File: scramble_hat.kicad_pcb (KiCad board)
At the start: 4 copper layers, 51.4 x 21.1 mm, 57 parts, among them J1 NCJ6FA-H, J2 TRRS PJ-3X4S (CTIA, bottom-si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, J3 Carrier LEFT 1-7, J4 Carrier RIGHT 1-7, J5 VDD_PoE / PGND, J6 I2C 3V3/AGND/SDA/SCL, K1 KAQY214S, K2 KAQY214S, Q1 DMP3098 (P-FET 60V), SW1 SS-12D00-G3, U1 ES8389, U2 TPS7A2033

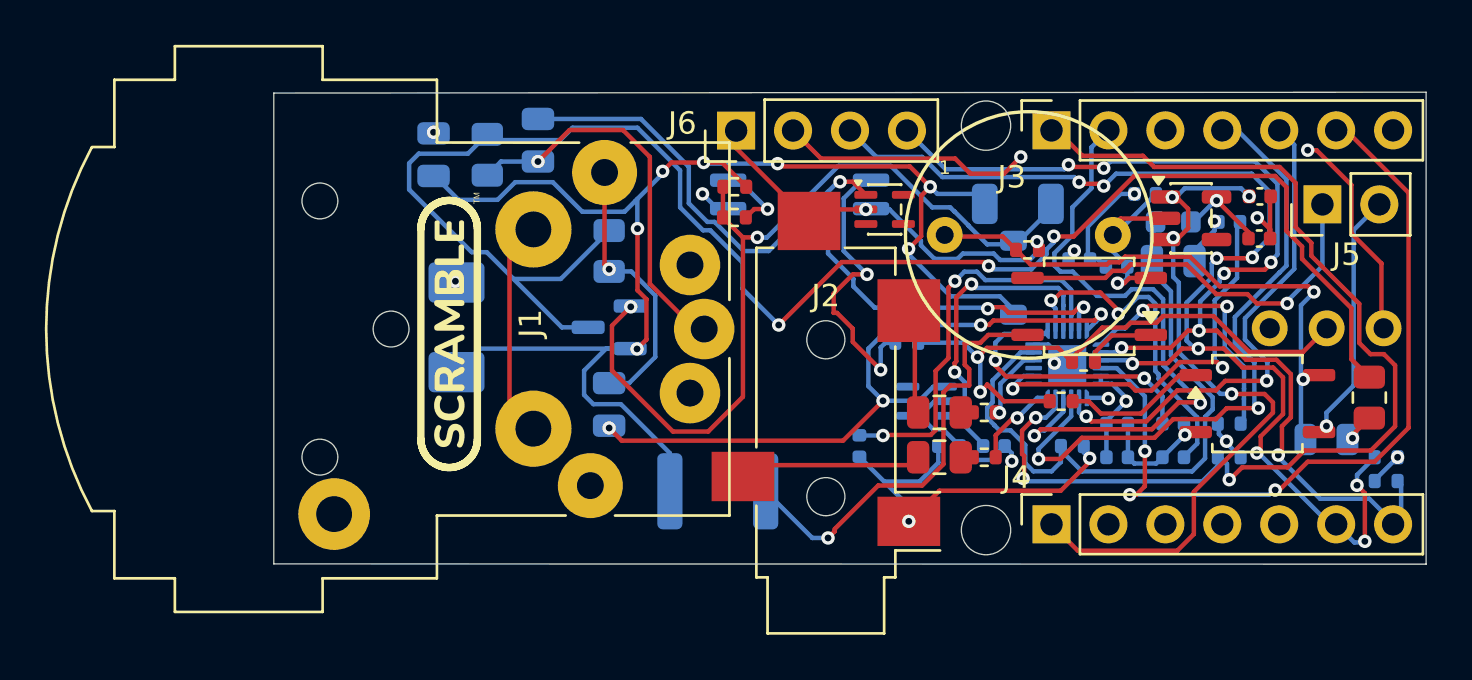
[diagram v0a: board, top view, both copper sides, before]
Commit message: pcb: place + route guitar input; regen fab
Layout for the guitar-input rev (U3 buffer, U4 mux, D9 tip ESD,
R19-R26/C23-C29, D1/D2 now SOD-323). Verified: DRC 0 errors /
0 unconnected, schematic sync clean (75 comps / 61 nets both sides).

Post-layout fixes:
- restore exclude_from_pos_files on C19/J1/J2/J5 (wiped again by
  re-layout; CPL correctly excludes C19,J1,J2,J5,R14)
- point D9 at the project-local 3D model (stock lib ships none)
- remove stale OK1_LED_A routing left from the mis-wired-label detour
  (1 via + 10 segments, all dangling; net verified intact throughout)

fab/ regenerated: gerbers/drills/zip, BOM 34 assembled, CPL 70 placed.
Order-time checks in the JLCPCB preview: U1 QFN (+270) first, then U4
TSSOP-16 (no rotation pattern) and K1/K2 SOP-4 (-90). D1/D2/D9 are
bidirectional two-terminal parts - rotation is not a concern.
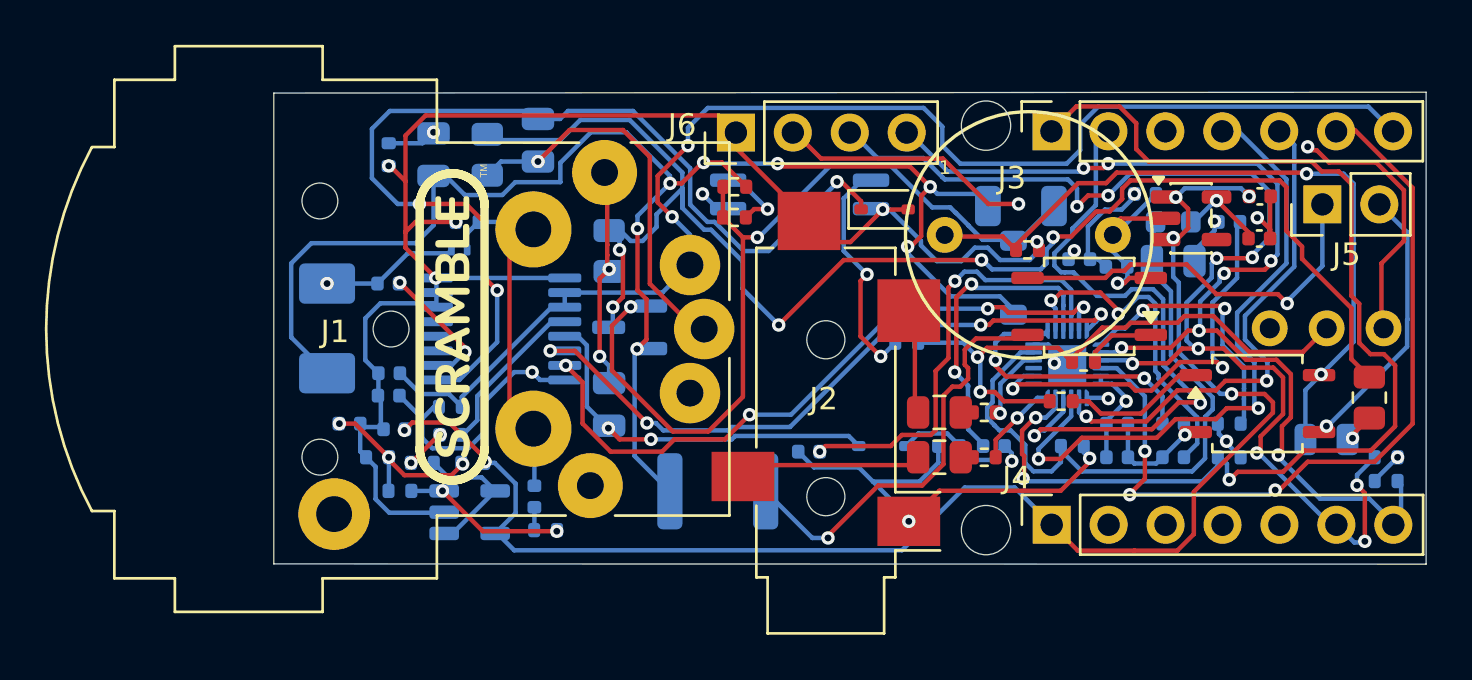
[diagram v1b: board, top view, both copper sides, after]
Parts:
- added C23: 1uF, Capacitor_SMD:C_0402_1005Metric, B.Cu at (92.5, 98.2)
- added C24: 1uF, Capacitor_SMD:C_0402_1005Metric, B.Cu at (84.2, 95.0)
- added C25: 1uF, Capacitor_SMD:C_0402_1005Metric, B.Cu at (88.8, 95.5)
- added C26: 1uF, Capacitor_SMD:C_0402_1005Metric, B.Cu at (86.0, 88.8)
- added C27: 100nF, Capacitor_SMD:C_0402_1005Metric, B.Cu at (86.0, 92.8)
- added C28: 100nF, Capacitor_SMD:C_0402_1005Metric, B.Cu at (86.2, 95.2)
- added C29: 100nF, Capacitor_SMD:C_0402_1005Metric, B.Cu at (86.0, 93.8)
- added D9: TPD1E10B06 (ESD), Package_SON:Texas_DPY0002A_0.6x1mm_P0.65mm, B.Cu at (89.2, 87.2)
- added R19: 100k, Resistor_SMD:R_0402_1005Metric, B.Cu at (88.8, 94.2)
- added R20: 2.2k, Resistor_SMD:R_0402_1005Metric, B.Cu at (93.0, 99.8)
- added R21: 1M, Resistor_SMD:R_0402_1005Metric, B.Cu at (86.5, 98.0)
- added R22: 100k, Resistor_SMD:R_0402_1005Metric, B.Cu at (89.8, 96.8)
- added R23: 100k, Resistor_SMD:R_0402_1005Metric, B.Cu at (85.5, 96.5)
- added R24: 33R, Resistor_SMD:R_0402_1005Metric, B.Cu at (87.5, 96.8)
- added R25: 10k, Resistor_SMD:R_0402_1005Metric, B.Cu at (86.0, 83.0)
- added R26: 1M, Resistor_SMD:R_0402_1005Metric, B.Cu at (89.5, 86.0)
- added U3: TLV9061, Package_TO_SOT_SMD:SOT-23-5, B.Cu at (89.6, 99.0)
- added U4: 74HC4053, Package_SO:TSSOP-16_4.4x5mm_P0.65mm, B.Cu at (91.0, 90.8)
- D1, D2: value PESD3V3L4UF (ESD) -> PESD3V3L1BA (ESD); footprint Package_TO_SOT_SMD:SOT-353_SC-70-5 -> Diode_SMD:D_SOD-323
- moved D6 5.78 mm to (83.2, 90.8)
- moved D2 2.81 mm to (108.0, 96.0)
- moved C12 2.26 mm to (104.8, 96.2), turned to 0 degrees
- moved Q1 0.92 mm to (96.8, 90.7)
- moved C18 0.17 mm to (114.2, 85.3)
- moved J6 0.09 mm to (101.5, 82.0)
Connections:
- C10 pad 2: MIC1P -> MIC1P_XLR
- C11 pad 2: MIC1N -> MIC1N_XLR
- D1 pad 1: MIC1N -> MIC1N_XLR
- D2 pad 1: MIC1P -> MIC1P_XLR
- J1 pad R: unconnected-(J1-JACK_R-PadR) -> DET
- J1 pad T: unconnected-(J1-JACK_T-PadT) -> GTIP
- J3 pad 7: PHANTOM_EN -> DET
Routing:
- net DET: track 0.00 -> 59.6 mm, vias 0 -> 2
- net AGND: track 59.2 -> 113.9 mm, vias 12 -> 15
- net MIC1N_XLR: track 0.00 -> 45.0 mm, vias 0 -> 3
- net +5V: track 31.9 -> 67.7 mm, vias 4 -> 6
- net +3V3: track 22.5 -> 52.4 mm, vias 4 -> 5
- net MIC1P_XLR: track 0.00 -> 16.9 mm, vias 0 -> 2
- net PGND: track 26.3 -> 42.7 mm
- net GTIP: track 0.00 -> 15.5 mm
- net V_PHANTOM: track 75.7 -> 66.0 mm, vias 3 -> 5
- net unconnected-(J1-JACK_T-PadT): track 8.89 -> 0.00 mm
- net VBIAS: track 0.00 -> 8.34 mm, vias 0 -> 3
- net GB_IN: track 0.00 -> 7.36 mm, vias 0 -> 2
- net BUF_AC: track 0.00 -> 7.35 mm
- net MIC1N: track 36.3 -> 29.8 mm, vias 3 -> 4
- net BUF_OUT: track 0.00 -> 6.32 mm
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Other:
- board text added: "1/4{dblquote} XLR"
- board text added: "Hat-trik v3"
- board text added: "PHANTOM"
- board text added: "TRRS"
- board text removed: "Hat-trik v2"
- board text removed: "PHTM PWR"
- board text removed: "TRRS JACK"
- board text removed: "XLR + 1/4{dblquote} INPUT"

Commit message: pcb: minor route/silk tweaks; regen fab + doc PDFs
Bottom-side route touch-ups and silk adjustments after the guitar-input
layout. Verified: DRC 0 errors / 0 unconnected, schematic sync clean.
fab/ regenerated (CPL 70 placed, excludes C19/J1/J2/J5/R14; zip rebuilt
to match); docs/ schematic + top/bottom silk PDFs refreshed for the
guitar-input rev.
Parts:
- moved C29 0.12 mm to (85.9, 93.8)
- moved C27 0.09 mm to (85.9, 92.7)
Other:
- board text added: "+ -"
- board text added: "1/4{dblquote} +XLR"
- board text added: "5V"
- board text added: "GND-3V3-SCL-SDA"
- board text added: "PoE"
- board text removed: "1/4{dblquote} XLR"
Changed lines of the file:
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@@
 		(tags "Through hole socket strip THT 1x07 2.54mm single row")
 		(property "Reference" "J3"
-			(at -2.085 -1.77 0)
+			(at -2.541486 -1.568642 0)
 			(layer "F.SilkS")
 			(effects
@@
 		(tags "Through hole pin header THT 1x04 2.54mm single row")
 		(property "Reference" "J6"
-			(at 0.324935 -2.400153 0)
+			(at -2.285465 -1.59018 0)
 			(layer "F.SilkS")
 			(effects
@@
 		(tags "Through hole pin header THT 1x02 2.54mm single row")
 		(property "Reference" "J5"
-			(at -2.2352 1.0718 0)
+			(at -2.483 -1.2554 0)
 			(layer "F.SilkS")
 			(effects
@@
 		)
 		(fp_text user "1"
-			(at -3.75 -3 0)
+			(at -3.755869 1.518742 0)
 			(layer "F.SilkS")
 			(effects
@@
 	(footprint "Capacitor_SMD:C_0402_1005Metric"
 		(layer "B.Cu")
-		(at 86.02 92.75 180)
+		(at 85.929072 92.749154 180)
 		(descr "Capacitor SMD 0402 (1005 Metric), square (rectangular) end terminal, IPC-7351 nominal, (Body size source: IPC-SM-782 page 76, https://www.pcb-3d.com/wordpress/wp-content/uploads/ipc-sm-782a_amendment_1_and_2.pdf)")
 		(tags "capacitor")
@@
 	(footprint "Capacitor_SMD:C_0402_1005Metric"
 		(layer "B.Cu")
-		(at 86 93.75 180)
+		(at 85.929072 93.841562 180)
 		(descr "Capacitor SMD 0402 (1005 Metric), square (rectangular) end terminal, IPC-7351 nominal, (Body size source: IPC-SM-782 page 76, https://www.pcb-3d.com/wordpress/wp-content/uploads/ipc-sm-782a_amendment_1_and_2.pdf)")
 		(tags "capacitor")
@@
 		(layer "F.SilkS")
 	)
+	(gr_line
+		(start 116 97)
+		(end 116 98)
+		(stroke
+			(width 0.1)
+			(type default)
+		)
+		(layer "F.SilkS")
+	)
+	(gr_line
+		(start 116.84967 96.5)
+		(end 116 97)
+		(stroke
+			(width 0.1)
+			(type default)
+		)
+		(layer "F.SilkS")
+	)
 	(gr_poly
 		(pts
@@
 		(layer "Edge.Cuts")
 	)
+	(gr_text "+ -"
+		(at 127.4 87.6 0)
+		(layer "F.SilkS")
+		(effects
+			(font
+				(size 1 1)
+				(thickness 0.1)
+			)
+			(justify left bottom)
+		)
+	)
+	(gr_text "GND-3V3-SCL-SDA"
+		(at 92.2 81.3 0)
+		(layer "F.SilkS")
+		(effects
+			(font
+				(size 1 1)
+				(thickness 0.1)
+			)
+		)
+	)
+	(gr_text "5V"
+		(at 117.4 95.8 0)
+		(layer "F.SilkS")
+		(effects
+			(font
+				(size 1 1)
+				(thickness 0.1)
+			)
+		)
+	)
+	(gr_text "PoE"
+		(at 129.5 88.4 0)
+		(layer "F.SilkS")
+		(effects
+			(font
+				(size 1 1)
+				(thickness 0.1)
+			)
+		)
+	)
 	(gr_text "TRRS"
 		(at 107.3 100.8 0)
@@
 		)
 	)
-	(gr_text "1/4{dblquote}\nXLR"
-		(at 81.3 82.2 270)
+	(gr_text "1/4{dblquote}\n+XLR"
+		(at 81.5 82.4 270)
 		(layer "B.SilkS")
 		(effects
@@
 	)
 	(segment
+		(start 84.956 90.303254)
+		(end 84.956 92.166)
+		(width 0.2)
+		(layer "B.Cu")
+		(net "AGND")
+	)
+	(segment
 		(start 114.922657 86.882682)
 		(end 114.918415 86.882682)
@@
 	)
 	(segment
+		(start 85.45 94.93)
+		(end 85.77 95.25)
+		(width 0.2)
+		(layer "B.Cu")
+		(net "AGND")
+	)
+	(segment
 		(start 118.98 96.5)
 		(end 118.98 95)
@@
 	)
 	(segment
-		(start 85.54 92.75)
-		(end 84.956 92.166)
-		(width 0.2)
-		(layer "B.Cu")
-		(net "AGND")
-	)
-	(segment
 		(start 119.2596 96.7796)
 		(end 118.98 96.5)
@@
 	)
 	(segment
-		(start 87.956444 89.6296)
-		(end 88.128709 89.801865)
-		(width 0.2)
-		(layer "B.Cu")
-		(net "AGND")
-	)
-	(segment
 		(start 86.025 98.975)
 		(end 85.416 98.366)
@@
 	)
 	(segment
-		(start 85.54 92.75)
-		(end 85.54 93.73)
-		(width 0.2)
-		(layer "B.Cu")
-		(net "AGND")
-	)
-	(segment
 		(start 110.45 87.75)
 		(end 109.7448 87.0448)
@@
 	)
 	(segment
-		(start 85.54 93.73)
-		(end 85.52 93.75)
-		(width 0.2)
-		(layer "B.Cu")
-		(net "AGND")
-	)
-	(segment
 		(start 111.55 87.75)
 		(end 110.45 87.75)
@@
 	(segment
 		(start 84.956 92.166)
-		(end 84.956 90.303254)
-		(width 0.2)
-		(layer "B.Cu")
-		(net "AGND")
-	)
-	(segment
-		(start 85.65 93.88)
-		(end 85.65 95.13)
+		(end 85.45 92.66)
 		(width 0.2)
 		(layer "B.Cu")
@@
 	)
 	(segment
-		(start 85.629654 89.6296)
-		(end 87.956444 89.6296)
-		(width 0.2)
-		(layer "B.Cu")
-		(net "AGND")
-	)
-	(segment
 		(start 93.853709 88.501865)
 		(end 88.128709 88.501865)
@@
 	)
 	(segment
-		(start 120.23 84.75)
-		(end 120.228563 84.75)
+		(start 85.629654 89.6296)
+		(end 84.956 90.303254)
 		(width 0.2)
 		(layer "B.Cu")
@@
 	)
 	(segment
-		(start 84.956 90.303254)
-		(end 85.629654 89.6296)
+		(start 120.23 84.75)
+		(end 120.228563 84.75)
 		(width 0.2)
 		(layer "B.Cu")
@@
 	)
 	(segment
+		(start 85.45 92.66)
+		(end 85.45 94.93)
+		(width 0.2)
+		(layer "B.Cu")
+		(net "AGND")
+	)
+	(segment
 		(start 123.0376 95.0476)
 		(end 122.99 95)
@@
 	)
 	(segment
-		(start 85.65 95.13)
-		(end 85.77 95.25)
+		(start 109.7448 86.8448)
+		(end 108.342625 85.442625)
 		(width 0.2)
 		(layer "B.Cu")
@@
 	)
 	(segment
-		(start 109.7448 86.8448)
-		(end 108.342625 85.442625)
+		(start 87.956444 89.6296)
+		(end 85.629654 89.6296)
 		(width 0.2)
 		(layer "B.Cu")
@@
 	)
 	(segment
-		(start 85.52 93.75)
-		(end 85.65 93.88)
+		(start 113.8008 96.6724)
+		(end 113.8008 96.3208)
 		(width 0.2)
 		(layer "B.Cu")
@@
 	)
 	(segment
-		(start 113.8008 96.6724)
-		(end 113.8008 96.3208)
+		(start 108.342625 85.442625)
+		(end 108.04 85.442625)
 		(width 0.2)
 		(layer "B.Cu")
@@
 	)
 	(segment
-		(start 108.342625 85.442625)
-		(end 108.04 85.442625)
+		(start 88.128709 89.801865)
+		(end 87.956444 89.6296)
 		(width 0.2)
 		(layer "B.Cu")
@@
 	)
 	(segment
+		(start 88.69 93.68)
+		(end 89.26 94.25)
+		(width 0.2)
+		(layer "B.Cu")
+		(net "DET")
+	)
+	(segment
 		(start 93.268463 89.801865)
 		(end 89.26 93.810328)
@@
 	)
 	(segment
+		(start 86.5 92.75)
+		(end 86.5 92.845)
+		(width 0.2)
+		(layer "B.Cu")
+		(net "DET")
+	)
+	(segment
 		(start 99.35 81.8)
 		(end 100.235465 80.914535)
@@
 	)
 	(segment
+		(start 86.5 92.845)
+		(end 87.335 93.68)
+		(width 0.2)
+		(layer "B.Cu")
+		(net "DET")
+	)
+	(segment
 		(start 110.7 81.75)
 		(end 110.7 82.6)
@@
 	)
 	(segment
+		(start 87.335 93.68)
+		(end 88.69 93.68)
+		(width 0.2)
+		(layer "B.Cu")
+		(net "DET")
+	)
+	(segment
 		(start 116.85 81.661521)
 		(end 117.653007 80.858514)
@@
 	)
 	(segment
-		(start 86.5 92.75)
-		(end 87.43 93.68)
-		(width 0.2)
-		(layer "B.Cu")
-		(net "DET")
-	)
-	(segment
 		(start 89.26 93.810328)
 		(end 89.26 94.25)
@@
 	)
 	(segment
-		(start 88.69 93.68)
-		(end 89.26 94.25)
-		(width 0.2)
-		(layer "B.Cu")
-		(net "DET")
-	)
-	(segment
 		(start 109.864535 80.914535)
 		(end 110.7 81.75)
@@
 	)
 	(segment
-		(start 87.43 93.68)
-		(end 88.69 93.68)
-		(width 0.2)
-		(layer "B.Cu")
-		(net "DET")
-	)
-	(segment
 		(start 120.6581 84.8879)
 		(end 121.1337 84.8879)
@@
 	)
 	(segment
-		(start 87.5 94.77)
-		(end 86.48 93.75)
-		(width 0.2)
-		(layer "B.Cu")
-		(net "+3V3")
-	)
-	(segment
 		(start 129.99 97.52)
 		(end 131.01 96.5)
@@
 	)
 	(segment
+		(start 86.48 93.78)
+		(end 86.48 93.75)
+		(width 0.2)
+		(layer "B.Cu")
+		(net "+3V3")
+	)
+	(segment
 		(start 117.773 93.223)
 		(end 117.773 92.873)
@@
 	)
 	(segment
+		(start 87.5 94.77)
+		(end 87.47 94.77)
+		(width 0.2)
+		(layer "B.Cu")
+		(net "+3V3")
+	)
+	(segment
 		(start 92.4 92.7)
 		(end 92.751865 93.051865)
@@
 		(width 0.2)
 		(layer "B.Cu")
+		(net "+3V3")
+	)
+	(segment
+		(start 87.47 94.77)
+		(end 86.48 93.78)
+		(width 0.2)
+		(layer "B.Cu")

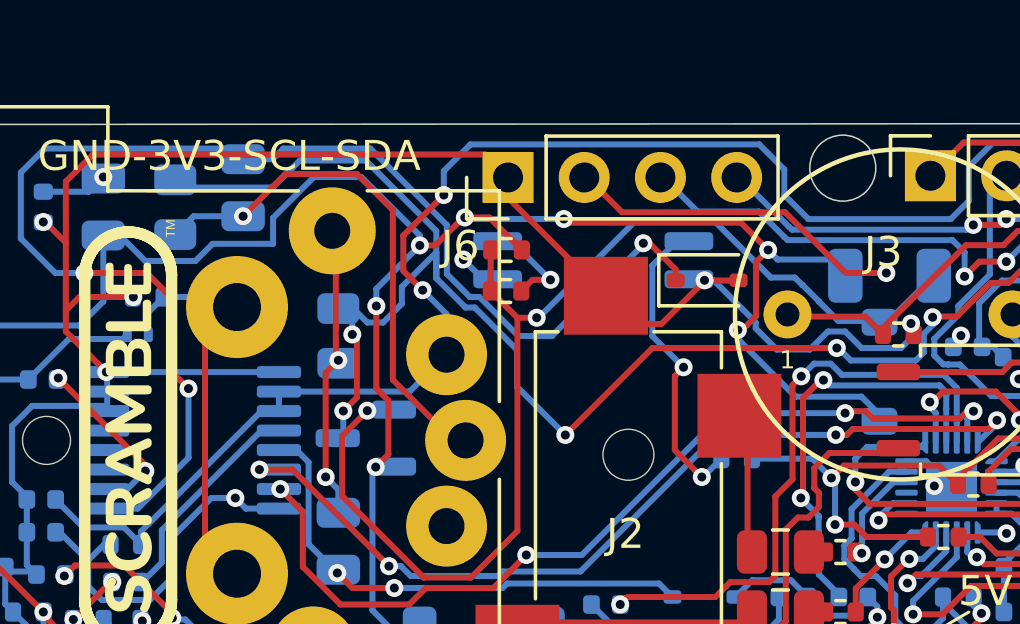
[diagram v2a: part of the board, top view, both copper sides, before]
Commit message: pcb: reroute V_PHANTOM away from MIC1N_XLR on B.Cu; regen fab + doc PDFs
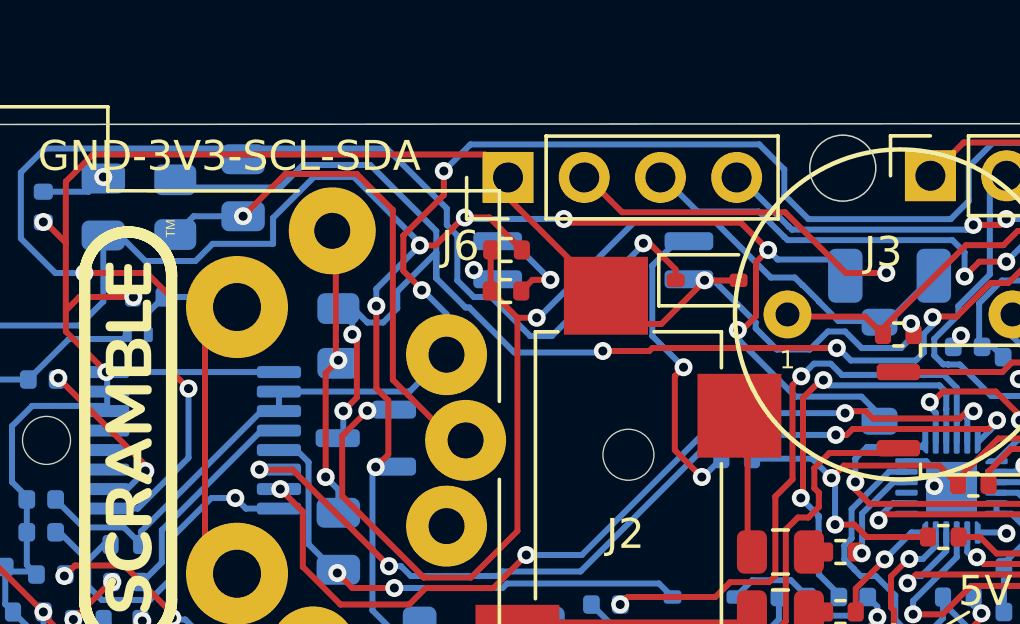
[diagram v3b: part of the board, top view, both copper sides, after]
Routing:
- net V_PHANTOM: track 66.0 -> 62.9 mm
